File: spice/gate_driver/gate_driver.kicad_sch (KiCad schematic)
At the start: 10 parts, among them U1 UCC27517, U2 UCC27517

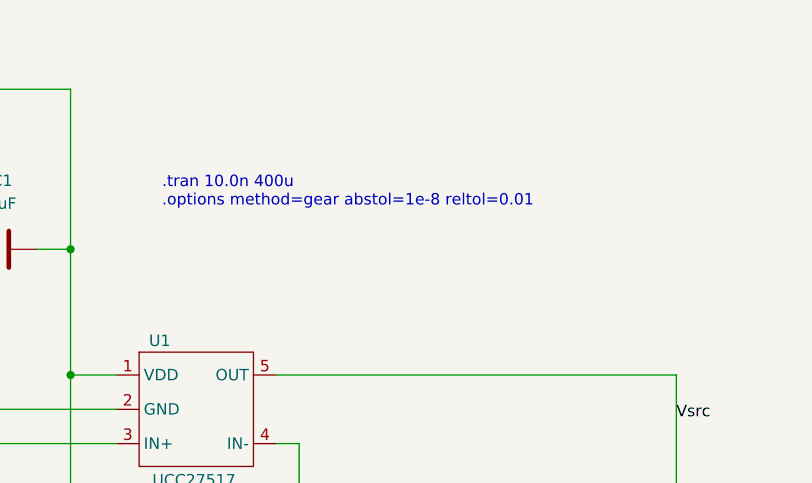
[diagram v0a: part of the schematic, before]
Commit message: Added notes about series termination resistors.
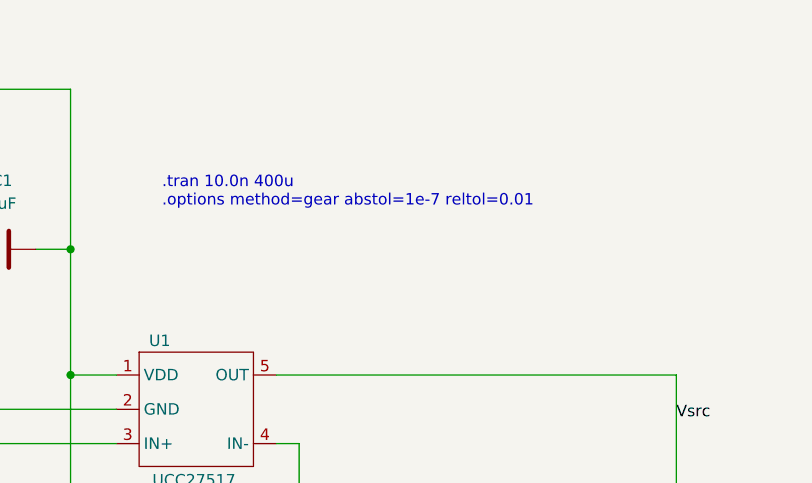
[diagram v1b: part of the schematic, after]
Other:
- note added: ".tran 10.0n 400u .options method=gear abstol=1e-7 reltol=0.01"
- note removed: ".tran 10.0n 400u .options method=gear abstol=1e-8 reltol=0.01"
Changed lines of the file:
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@@
 		)
 	)
-	(text ".tran 10.0n 400u\n.options method=gear abstol=1e-8 reltol=0.01"
+	(text ".tran 10.0n 400u\n.options method=gear abstol=1e-7 reltol=0.01"
 		(exclude_from_sim no)
 		(at 132.08 61.468 0)
@@
 			)
 		)
-		(property "Sim.Params" "is=23.4p rs=0 n=3.94"
+		(property "Sim.Params" "is=23.4p rs=0 n=3.94 cjo=0"
 			(at 189.23 115.57 0)
 			(effects
